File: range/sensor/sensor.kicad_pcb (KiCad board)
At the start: 2 copper layers, 35.6 x 27.9 mm, 7 parts

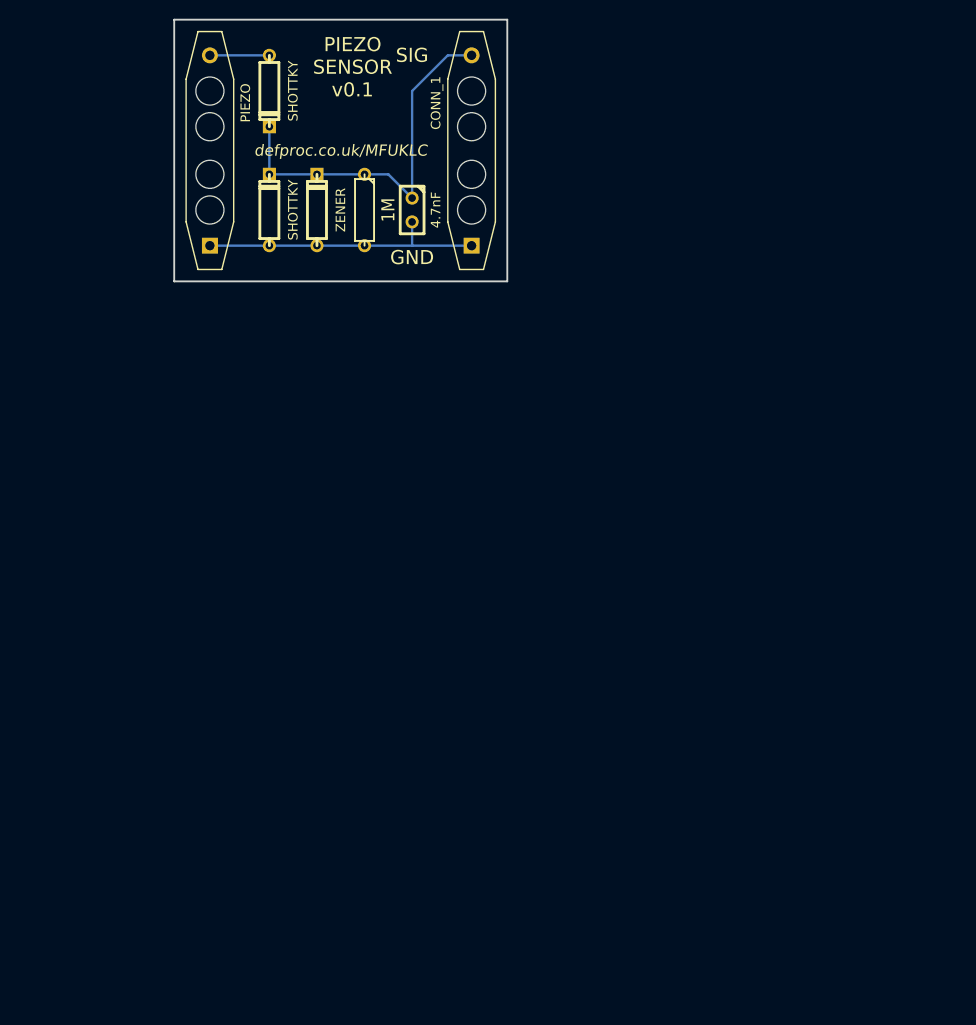
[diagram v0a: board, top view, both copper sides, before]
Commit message: revised sensor board, and removed previous gerbers
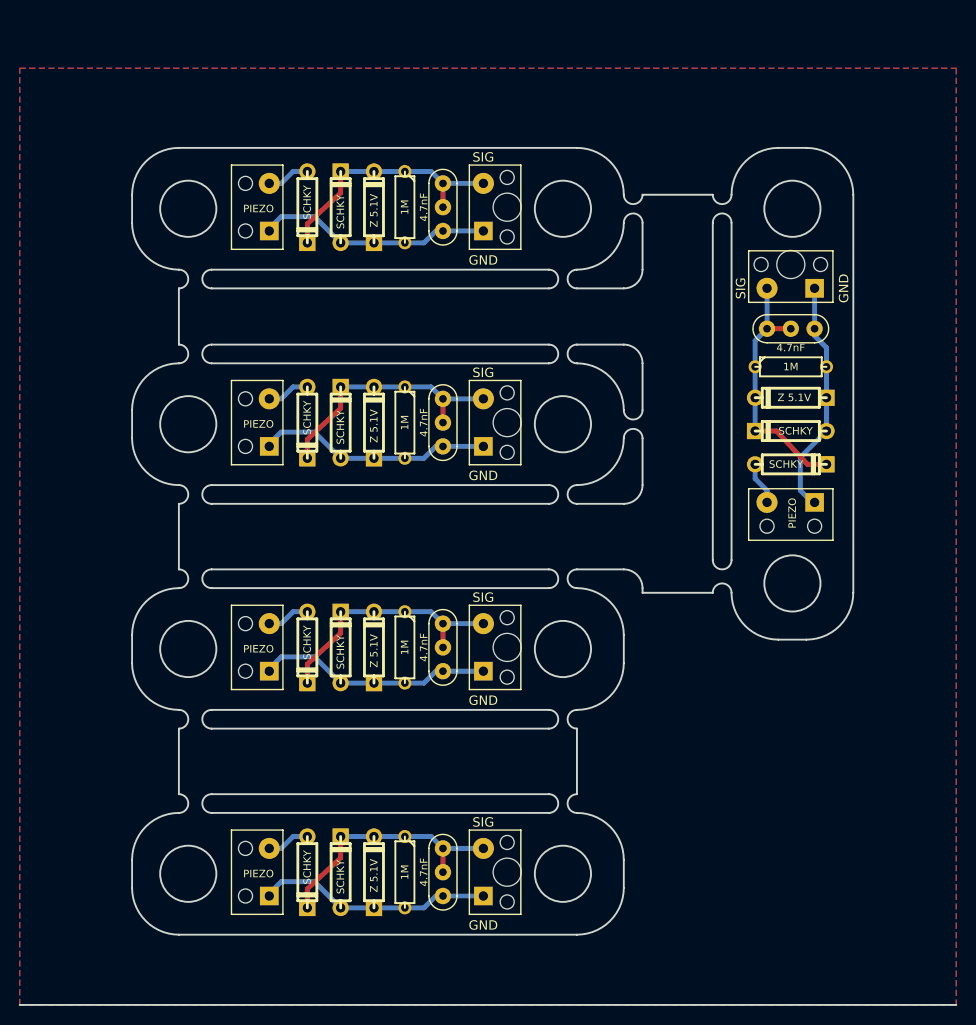
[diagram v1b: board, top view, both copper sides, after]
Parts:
- removed the PIEZO at (194.3, 144.8)
- added 4.7nF: 4.7nF, C1-2, F.Cu at (257.6, 163.8)
- added 4.7nF: 4.7nF, C1-2, F.Cu at (219.2, 223.1)
- added 4.7nF: 4.7nF, C1-2, F.Cu at (219.2, 199.1)
- added 4.7nF: 4.7nF, C1-2, F.Cu at (219.2, 175.1)
- added CONN: CONN_2, PZ1, F.Cu at (256.3, 159.5)
- added CONN: CONN_2, PZ1, F.Cu at (223.5, 221.8)
- added CONN: CONN_2, PZ1, F.Cu at (223.5, 197.8)
- added CONN: CONN_2, PZ1, F.Cu at (223.5, 173.8)
- added PIEZO: PIEZO, PZ2, F.Cu at (256.3, 184.9)
- added PIEZO: PIEZO, PZ2, F.Cu at (198.1, 221.8)
- added PIEZO: PIEZO, PZ2, F.Cu at (198.1, 197.8)
- added PIEZO: PIEZO, PZ2, F.Cu at (198.1, 173.8)
- added PIEZO: PIEZO, PZ2, F.Cu at (198.1, 150.8)
- added R1: 1M, R3, F.Cu at (256.3, 167.9)
- added R1: 1M, R3, F.Cu at (215.1, 221.8)
- added R1: 1M, R3, F.Cu at (215.1, 197.8)
- added R1: 1M, R3, F.Cu at (215.1, 173.8)
- added SCHKY: SHOTTKY DIODE SR1100, SCHKY1, F.Cu at (256.3, 178.3)
- added SCHKY: SHOTTKY DIODE SR1100, SCHKY1, F.Cu at (256.3, 174.7)
- added SCHKY: SHOTTKY DIODE SR1100, SCHKY1, F.Cu at (208.3, 221.8)
- added SCHKY: SHOTTKY DIODE SR1100, SCHKY1, F.Cu at (204.7, 221.8)
- added SCHKY: SHOTTKY DIODE SR1100, SCHKY1, F.Cu at (204.7, 197.8)
- added SCHKY: SHOTTKY DIODE SR1100, SCHKY1, F.Cu at (208.3, 197.8)
- added SCHKY: SHOTTKY DIODE SR1100, SCHKY1, F.Cu at (208.3, 173.8)
- added SCHKY: SHOTTKY DIODE SR1100, SCHKY1, F.Cu at (204.7, 173.8)
- added Z 5.1V: ZENER DIODE 1N751A, D3-REV, F.Cu at (256.3, 171.2)
- added Z 5.1V: ZENER DIODE 1N751A, D3-REV, F.Cu at (211.8, 221.8)
- added Z 5.1V: ZENER DIODE 1N751A, D3-REV, F.Cu at (211.8, 197.8)
- added Z 5.1V: ZENER DIODE 1N751A, D3-REV, F.Cu at (211.8, 173.8)
- 4.7nF: footprint C1 -> C1-2
- SCHKY (x2): renamed from SHOTTKY; footprint D3 -> SCHKY1
- Z 5.1V: renamed from ZENER; footprint D3 -> D3-REV
- moved SCHKY 13.0 mm to (204.7, 150.8)
- moved SCHKY 7.62 mm to (208.3, 150.8)
- moved CONN 6.18 mm to (223.5, 150.8)
- moved Z 5.1V 6.09 mm to (211.8, 150.8)
- moved R1 4.32 mm to (215.1, 150.8)
- moved 4.7nF 3.43 mm to (219.2, 152.1)
- renumbered CONN_1 to CONN
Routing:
- net SIGNAL: track 40.7 -> 137.4 mm
- net GND: track 30.5 -> 126.6 mm
- net N-000001: track 6.35 -> 23.0 mm
- added copper zone on B.Cu, net GND
- added copper zone on F.Cu, net GND
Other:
- board size 35.6 x 27.9 mm -> 100 x 91.5 mm
- net class GNDV added: clearance 0.52, trace_width 0.52, via_dia 1.2, via_drill 1
- board text added: "Piezo Sensor defproc.co.uk/MFUKLC rev. 2"
- board text removed: "PIEZO SENSOR v0.1"
- board text removed: "defproc.co.uk/MFUKLC"
